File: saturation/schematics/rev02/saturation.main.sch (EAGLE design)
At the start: 37 parts, among them IC1 TL084P, J1 IN, J2 OUT

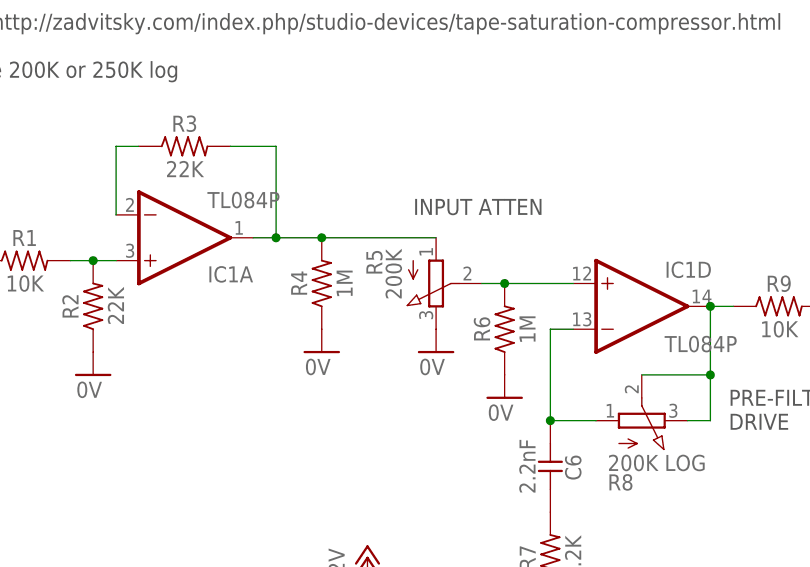
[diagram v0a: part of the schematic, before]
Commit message: Flipped sat atten pot
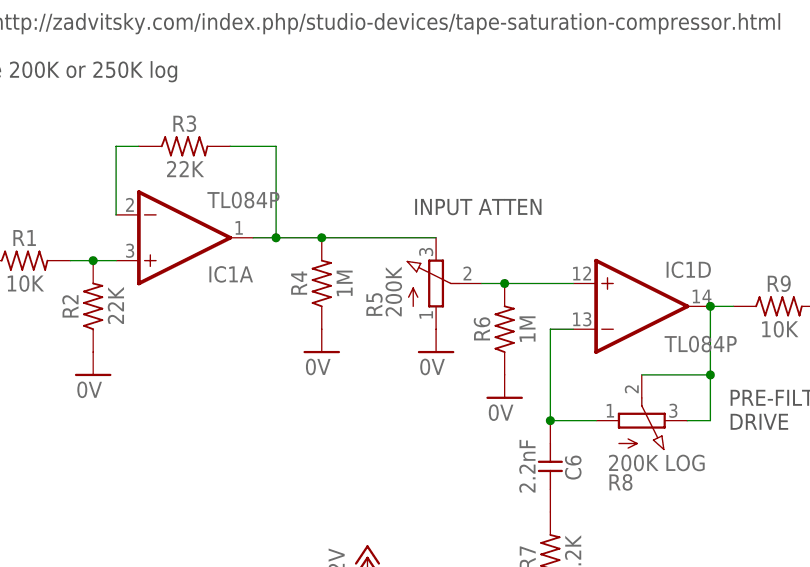
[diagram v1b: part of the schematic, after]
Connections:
- net 0V: now also R5.A; no longer R5.E
- net N$19: now also R5.E; no longer R5.A
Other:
- moved on the sheet: R5
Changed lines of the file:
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@@
 <?xml version="1.0" encoding="utf-8"?>
 <!DOCTYPE eagle SYSTEM "eagle.dtd">
-<eagle version="9.5.2">
+<eagle version="9.5.1">
 <drawing>
 <settings>
@@
 <attribute name="VALUE" x="113.03" y="77.47" size="1.778" layer="96"/>
 </instance>
-<instance part="R5" gate="G$1" x="7.62" y="88.9" smashed="yes" rot="MR180">
-<attribute name="NAME" x="1.651" y="92.71" size="1.778" layer="95" rot="MR270"/>
-<attribute name="VALUE" x="3.81" y="92.71" size="1.778" layer="96" rot="MR270"/>
+<instance part="R5" gate="G$1" x="7.62" y="88.9" smashed="yes">
+<attribute name="NAME" x="1.651" y="85.09" size="1.778" layer="95" rot="R90"/>
+<attribute name="VALUE" x="3.81" y="85.09" size="1.778" layer="96" rot="R90"/>
 </instance>
 <instance part="R8" gate="G$1" x="30.48" y="73.66" smashed="yes" rot="MR90">
@@
 <pinref part="R6" gate="G$1" pin="1"/>
 <pinref part="GND7" gate="1" pin="0V"/>
-</segment>
-<segment>
-<pinref part="R5" gate="G$1" pin="E"/>
-<pinref part="GND6" gate="1" pin="0V"/>
 </segment>
 <segment>
@@
 <pinref part="GND11" gate="1" pin="0V"/>
 </segment>
+<segment>
+<pinref part="R5" gate="G$1" pin="A"/>
+<pinref part="GND6" gate="1" pin="0V"/>
+</segment>
 </net>
 <net name="N$3" class="0">
@@
 <wire x1="-10.16" y1="93.98" x2="-5.08" y2="93.98" width="0.1524" layer="91"/>
 <junction x="-10.16" y="93.98"/>
-<pinref part="R5" gate="G$1" pin="A"/>
+<pinref part="R5" gate="G$1" pin="E"/>
 <wire x1="-5.08" y1="93.98" x2="7.62" y2="93.98" width="0.1524" layer="91"/>
 <junction x="-5.08" y="93.98"/>
@@
 <segment>
 <pinref part="R6" gate="G$1" pin="2"/>
+<pinref part="IC1" gate="D" pin="+IN"/>
+<wire x1="15.24" y1="88.9" x2="22.86" y2="88.9" width="0.1524" layer="91"/>
 <pinref part="R5" gate="G$1" pin="S"/>
 <wire x1="12.7" y1="88.9" x2="15.24" y2="88.9" width="0.1524" layer="91"/>
-<pinref part="IC1" gate="D" pin="+IN"/>
-<wire x1="15.24" y1="88.9" x2="22.86" y2="88.9" width="0.1524" layer="91"/>
 <junction x="15.24" y="88.9"/>
 </segment>
